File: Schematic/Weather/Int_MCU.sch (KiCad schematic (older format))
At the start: 9 parts, among them U1 AMS1117, U2 ESP-01v090

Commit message: new M_Board internal
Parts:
- removed C1, C3: 47uF, Capacitor_THT:CP_Radial_Tantal_D5.0mm_P2.50mm, symbol Device:CP
- removed C2: 0.1uF, Capacitor_THT:C_Disc_D3.8mm_W2.6mm_P2.50mm, symbol Device:C
- removed H17, H18: MountingHole_Pad, symbol Mechanical:MountingHole_Pad
- removed R1: 10k, Resistor_THT:R_Axial_DIN0207_L6.3mm_D2.5mm_P7.62mm_Horizontal, symbol Device:R
- removed R2: 4.7K, Resistor_THT:R_Axial_DIN0207_L6.3mm_D2.5mm_P7.62mm_Horizontal, symbol Device:R
- removed U1: AMS1117, Package_TO_SOT_SMD:SOT-223-3_TabPin2, symbol MyComponents:AMS1117
- added J10: Conn_02x04_Odd_Even, Connector_PinHeader_2.54mm:PinHeader_2x04_P2.54mm_Vertical, symbol Connector_Generic:Conn_02x04_Odd_Even
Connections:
- net J3_P2: now also U2.3 (CH_PD), J10.3 (Pin_3); no longer U2.6 (GPIO0)
- net J3_P3: now also J10.4 (Pin_4)
- net at U2.1 (UTXD): now also J10.1 (Pin_1)
- net J3_P4: now reaches U2.5 (RST)
- net J3_P4: now also J10.5 (Pin_5)
- net J3_P6: now reaches U2.7 (VCC)
- net J3_P6: now also J10.7 (Pin_7)
- net at U2.8 (URXD): now also J10.8 (Pin_8)
- net J2_P1 renamed J3_P1
- net J3_P1: now also J10.2 (Pin_2)
- new net J3_P5: J10.6 (Pin_6), U2.6 (GPIO0)
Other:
- moved on the sheet: U2

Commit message: more changes
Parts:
- renumbered J10 to J1, U2 to U1
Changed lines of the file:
@@
 $Descr A4 11693 8268
 encoding utf-8
-Sheet 3 14
+Sheet 3 15
 Title ""
 Date ""
@@
 P 5150 2500
 AR Path="/5C9306F6" Ref="U?"  Part="1"
-AR Path="/5C9253D5/5C9306F6" Ref="U2"  Part="1"
-F 0 "U2" H 5150 3015 50  0000 C CNN
+AR Path="/5C9253D5/5C9306F6" Ref="U1"  Part="1"
+F 0 "U1" H 5150 3015 50  0000 C CNN
 F 1 "ESP-01v090" H 5150 2924 50  0000 C CNN
 F 2 "footprint:ESP-01" H 5150 2500 50  0001 C CNN
@@
 $EndComp
 $Comp
-L Connector_Generic:Conn_02x04_Odd_Even J10
+L Connector_Generic:Conn_02x04_Odd_Even J1
 U 1 1 5CB1B851
 P 5000 3700
-F 0 "J10" H 5050 4017 50  0000 C CNN
+F 0 "J1" H 5050 4017 50  0000 C CNN
 F 1 "Conn_02x04_Odd_Even" H 5050 3926 50  0000 C CNN
 F 2 "Connector_PinHeader_2.54mm:PinHeader_2x04_P2.54mm_Vertical" H 5000 3700 50  0001 C CNN

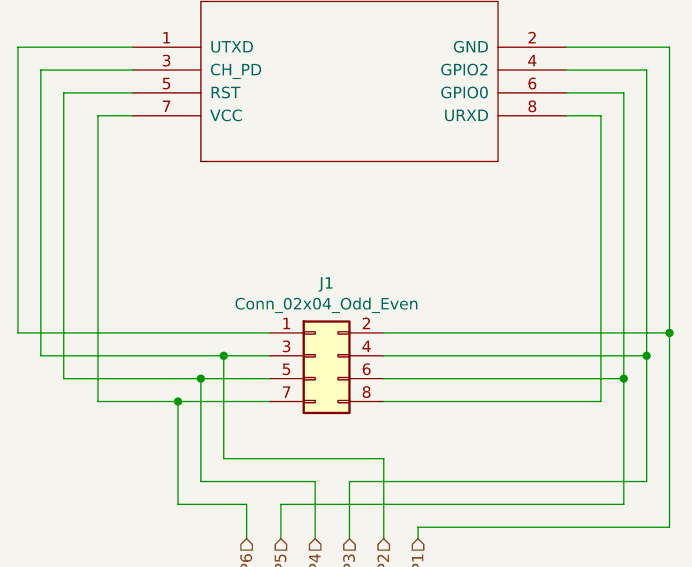
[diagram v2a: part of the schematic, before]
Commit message: Connector relable start
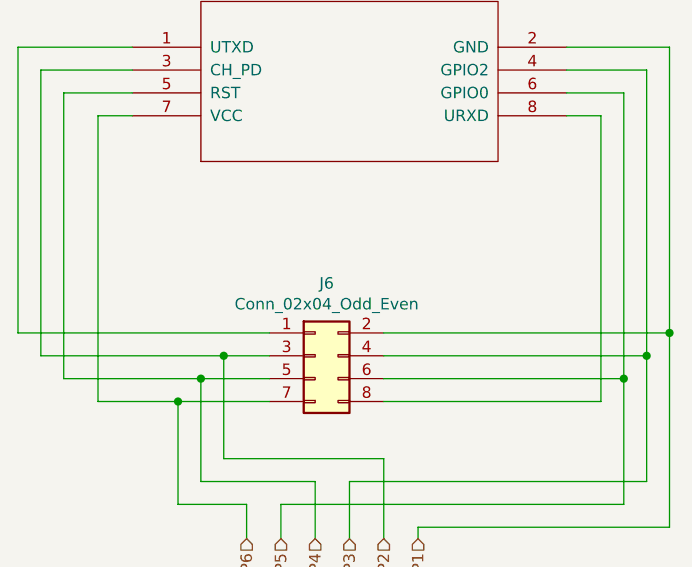
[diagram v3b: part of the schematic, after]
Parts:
- renumbered J1 to J6
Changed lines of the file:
@@
 $EndComp
 $Comp
-L Connector_Generic:Conn_02x04_Odd_Even J1
+L Connector_Generic:Conn_02x04_Odd_Even J6
 U 1 1 5CB1B851
 P 5000 3700
-F 0 "J1" H 5050 4017 50  0000 C CNN
+F 0 "J6" H 5050 4017 50  0000 C CNN
 F 1 "Conn_02x04_Odd_Even" H 5050 3926 50  0000 C CNN
 F 2 "Connector_PinHeader_2.54mm:PinHeader_2x04_P2.54mm_Vertical" H 5000 3700 50  0001 C CNN

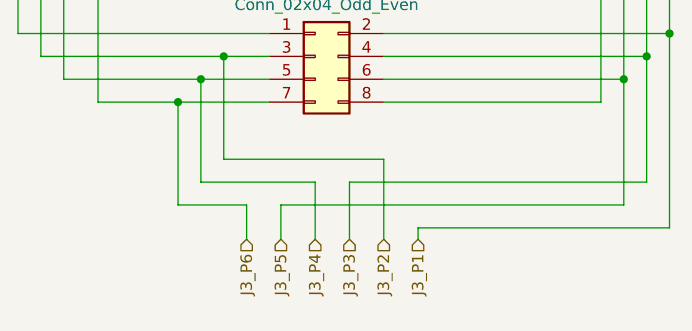
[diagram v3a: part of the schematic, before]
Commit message: Connector changes
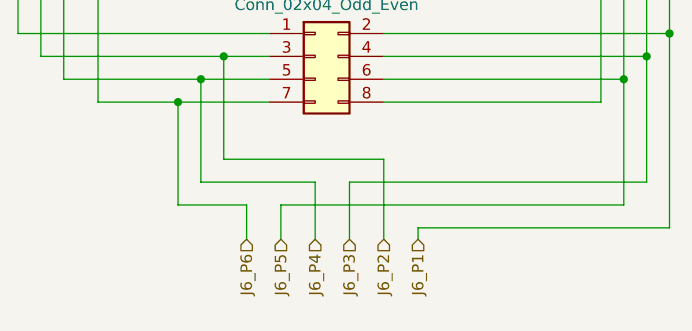
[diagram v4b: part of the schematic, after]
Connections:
- net J3_P1 renamed J6_P1
- net J3_P2 renamed J6_P2
- net J3_P3 renamed J6_P3
- net J3_P4 renamed J6_P4
- net J3_P5 renamed J6_P5
- net J3_P6 renamed J6_P6
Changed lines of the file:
@@
 $EndDescr
 Text HLabel 4700 4500 3    50   Input ~ 0
-J3_P6
+J6_P6
 Text HLabel 4850 4500 3    50   Input ~ 0
-J3_P5
+J6_P5
 Text HLabel 5450 4500 3    50   Input ~ 0
-J3_P1
+J6_P1
 Text HLabel 5300 4500 3    50   Input ~ 0
-J3_P2
+J6_P2
 Text HLabel 5150 4500 3    50   Input ~ 0
-J3_P3
+J6_P3
 Text HLabel 5000 4500 3    50   Input ~ 0
-J3_P4
+J6_P4
 $Comp
 L Weather-rescue:ESP-01v090-ESP8266 U?

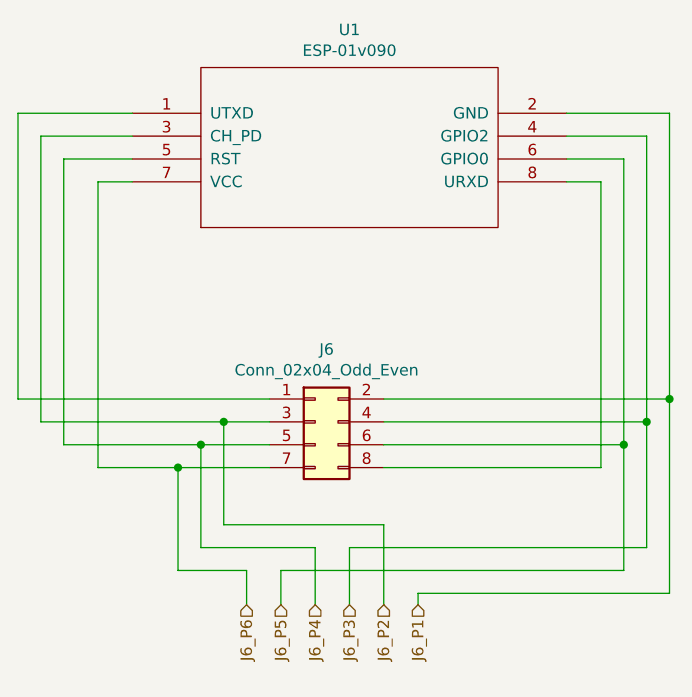
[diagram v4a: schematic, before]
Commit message: Local webpage added
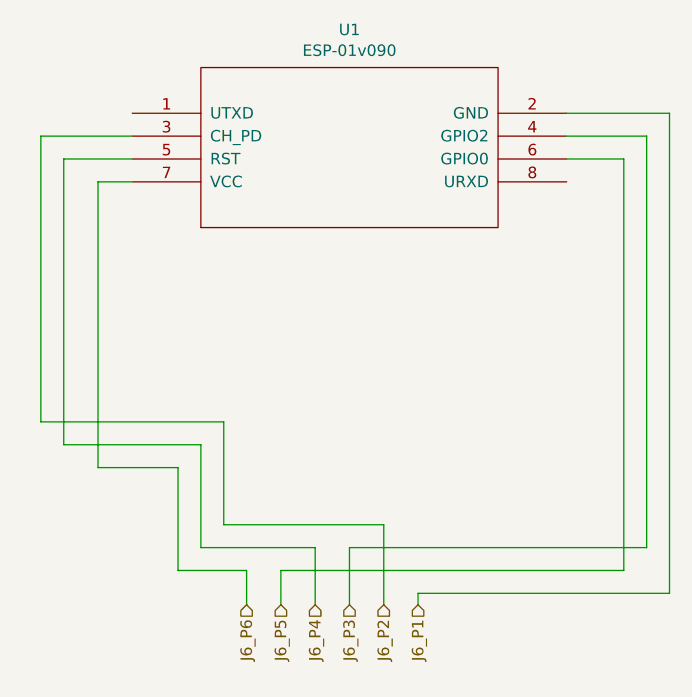
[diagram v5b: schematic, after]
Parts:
- removed J6: Conn_02x04_Odd_Even, Connector_PinHeader_2.54mm:PinHeader_2x04_P2.54mm_Vertical, symbol Connector_Generic:Conn_02x04_Odd_Even
- removed U1: ESP-01v090, footprint:ESP-01, symbol Weather-rescue:ESP-01v090-ESP8266
- added U1: ESP-01v090, footprint:ESP-01, symbol ESP8266:ESP-01v090
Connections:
- net J6_P1: now also U1.2 (GND)
- net J6_P2: now also U1.3 (CH_PD)
- net J6_P3: now also U1.4 (GPIO2)
- net J6_P4: now also U1.5 (RST)
- net J6_P5: now also U1.6 (GPIO0)
- net J6_P6: now also U1.7 (VCC)
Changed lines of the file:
@@
 Text HLabel 5000 4500 3    50   Input ~ 0
 J6_P4
+Wire Wire Line
+	3800 3700 3800 2450
+Wire Wire Line
+	3800 2450 4200 2450
+Wire Wire Line
+	3900 3800 3900 2550
+Wire Wire Line
+	3900 2550 4200 2550
+Wire Wire Line
+	4050 3900 4050 2650
+Wire Wire Line
+	4050 2650 4200 2650
+Wire Wire Line
+	6100 2550 6350 2550
+Wire Wire Line
+	6100 2450 6450 2450
+Wire Wire Line
+	6100 2350 6550 2350
+Wire Wire Line
+	4700 4500 4700 4350
+Wire Wire Line
+	4700 4350 4400 4350
+Wire Wire Line
+	4400 4350 4400 3900
+Wire Wire Line
+	4400 3900 4050 3900
+Wire Wire Line
+	4850 4500 4850 4350
+Wire Wire Line
+	4850 4350 6350 4350
+Wire Wire Line
+	5000 4500 5000 4250
+Wire Wire Line
+	5000 4250 4500 4250
+Wire Wire Line
+	4500 4250 4500 3800
+Wire Wire Line
+	4500 3800 3900 3800
+Wire Wire Line
+	5150 4500 5150 4250
+Wire Wire Line
+	5150 4250 6450 4250
+Wire Wire Line
+	5300 4500 5300 4150
+Wire Wire Line
+	5300 4150 4600 4150
+Wire Wire Line
+	4600 4150 4600 3700
+Wire Wire Line
+	4600 3700 3800 3700
+Wire Wire Line
+	5450 4500 5450 4450
+Wire Wire Line
+	5450 4450 6550 4450
+Wire Wire Line
+	6550 2350 6550 4450
+Wire Wire Line
+	6450 2450 6450 4250
+Wire Wire Line
+	6350 2550 6350 4350
 $Comp
-L Weather-rescue:ESP-01v090-ESP8266 U?
-U 1 1 5C9306F6
+L ESP8266:ESP-01v090 U1
+U 1 1 5CB3807E
 P 5150 2500
-AR Path="/5C9306F6" Ref="U?"  Part="1"
-AR Path="/5C9253D5/5C9306F6" Ref="U1"  Part="1"
 F 0 "U1" H 5150 3015 50  0000 C CNN
 F 1 "ESP-01v090" H 5150 2924 50  0000 C CNN
@@
 	1    0    0    -1
 $EndComp
-$Comp
-L Connector_Generic:Conn_02x04_Odd_Even J6
-U 1 1 5CB1B851
-P 5000 3700
-F 0 "J6" H 5050 4017 50  0000 C CNN
-F 1 "Conn_02x04_Odd_Even" H 5050 3926 50  0000 C CNN
-F 2 "Connector_PinHeader_2.54mm:PinHeader_2x04_P2.54mm_Vertical" H 5000 3700 50  0001 C CNN
-F 3 "~" H 5000 3700 50  0001 C CNN
-	1    5000 3700
-	1    0    0    -1
-$EndComp
-Wire Wire Line
-	3700 3600 3700 2350
-Wire Wire Line
-	3700 2350 4200 2350
-Wire Wire Line
-	4800 3700 4600 3700
-Wire Wire Line
-	3800 3700 3800 2450
-Wire Wire Line
-	3800 2450 4200 2450
-Wire Wire Line
-	4800 3800 4500 3800
-Wire Wire Line
-	3900 3800 3900 2550
-Wire Wire Line
-	3900 2550 4200 2550
-Wire Wire Line
-	4800 3900 4400 3900
-Wire Wire Line
-	4050 3900 4050 2650
-Wire Wire Line
-	4050 2650 4200 2650
-Wire Wire Line
-	6100 2650 6250 2650
-Wire Wire Line
-	6250 2650 6250 3900
-Wire Wire Line
-	6250 3900 5300 3900
-Wire Wire Line
-	6100 2550 6350 2550
-Wire Wire Line
-	6350 2550 6350 3800
-Wire Wire Line
-	6350 3800 5300 3800
-Wire Wire Line
-	6100 2450 6450 2450
-Wire Wire Line
-	6450 2450 6450 3700
-Wire Wire Line
-	6450 3700 5300 3700
-Wire Wire Line
-	6100 2350 6550 2350
-Wire Wire Line
-	6550 2350 6550 3600
-Wire Wire Line
-	6550 3600 5300 3600
-Wire Wire Line
-	4800 3600 3700 3600
-Wire Wire Line
-	4700 4500 4700 4350
-Wire Wire Line
-	4700 4350 4400 4350
-Wire Wire Line
-	4400 4350 4400 3900
-Connection ~ 4400 3900
-Wire Wire Line
-	4400 3900 4050 3900
-Wire Wire Line
-	4850 4500 4850 4350
-Wire Wire Line
-	4850 4350 6350 4350
-Wire Wire Line
-	6350 4350 6350 3800
-Connection ~ 6350 3800
-Wire Wire Line
-	5000 4500 5000 4250
-Wire Wire Line
-	5000 4250 4500 4250
-Wire Wire Line
-	4500 4250 4500 3800
-Connection ~ 4500 3800
-Wire Wire Line
-	4500 3800 3900 3800
-Wire Wire Line
-	5150 4500 5150 4250
-Wire Wire Line
-	5150 4250 6450 4250
-Wire Wire Line
-	6450 4250 6450 3700
-Connection ~ 6450 3700
-Wire Wire Line
-	5300 4500 5300 4150
-Wire Wire Line
-	5300 4150 4600 4150
-Wire Wire Line
-	4600 4150 4600 3700
-Connection ~ 4600 3700
-Wire Wire Line
-	4600 3700 3800 3700
-Wire Wire Line
-	5450 4500 5450 4450
-Wire Wire Line
-	5450 4450 6550 4450
-Wire Wire Line
-	6550 4450 6550 3600
-Connection ~ 6550 3600
 $EndSCHEMATC
